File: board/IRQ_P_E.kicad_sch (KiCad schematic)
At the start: 8 parts, among them U60 CY7C192-25, U61 CY7C192-25, U85 ATF22V10C-10PU, U86 ATF22V10C-10PU

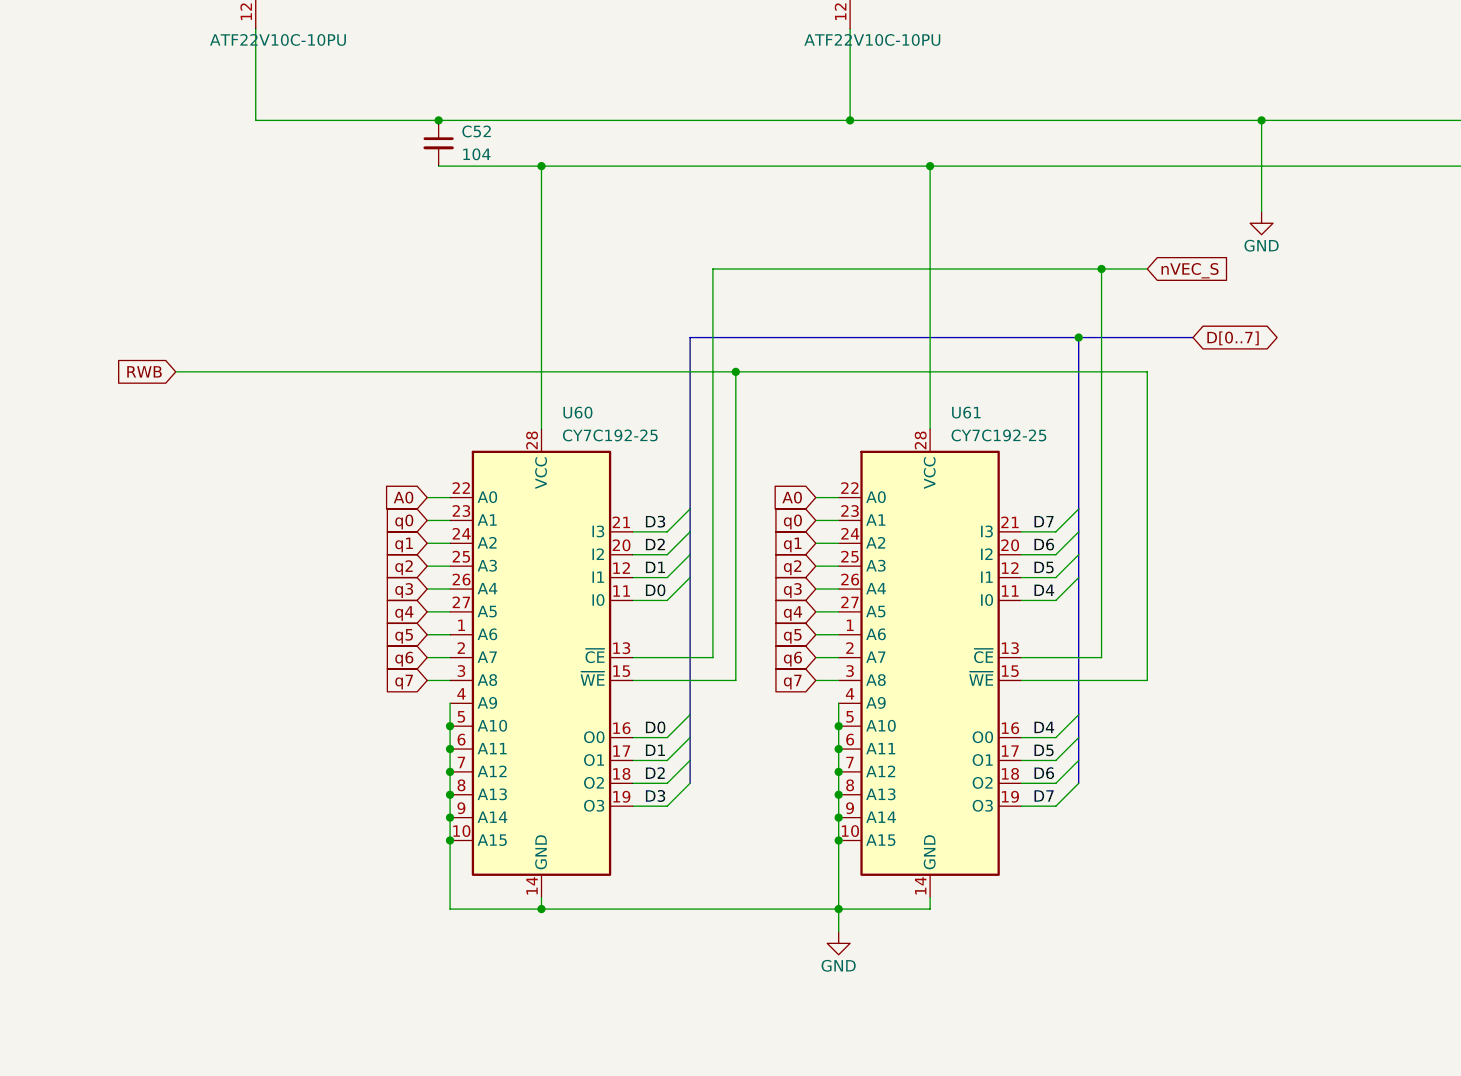
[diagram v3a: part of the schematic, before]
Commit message: V2.0: consolidate parts (239 -> 216), GAL C rev 02
No change in function:
- U9 74F08 removed: GAL C (U88) rev 02 makes the CPU phi0 (P_PHI0 = PHI2
  held low while DMAB_S is low); its decoupling cap C14 removed
- U34 74ACT14 removed: the two clock buffers use spare U19 74F240 gates
- U60 + U61 (2 x CY7C192 vector RAM) replaced by one AS7C256B-15
  (32K x 8, 15 ns); the IRQ sheet's D[0..7] bus is gone
- Crystal oscillators (U75 74HCU04, Y1, Y2, R1, R6-R8, C43, C44, C96,
  C97) replaced by canned oscillators X1 (14.31818 MHz), X2 (1.8432 MHz)
- Soft power: CD40106 -> 74HC14, CD4013 -> 74HC74 (active-low set/reset,
  power-on reset network inverted); a spare 74HC14 gate drives PS_ON#,
  so Q1 is removed
- R10-R13 -> RN6 (4 x 10k, SIP-5); R9, R21-R24 -> RN7 (5 x 33R isolated,
  SIP-10)
- C100-C102 (3 x 220u) -> C100 680u
- Clocks and Power sheet notes updated; PLD README updated

GAL C rev 02 verified against rev 01 over 200,000 clock edges.
PCB updated from the schematic (adds RN6, RN7, X1, X2 and the speakers
LS1/LS2). Also includes KiCad's re-save of the schematic sheets.

Co-Authored-By: Claude Opus 5.5 <noreply@anthropic.com>
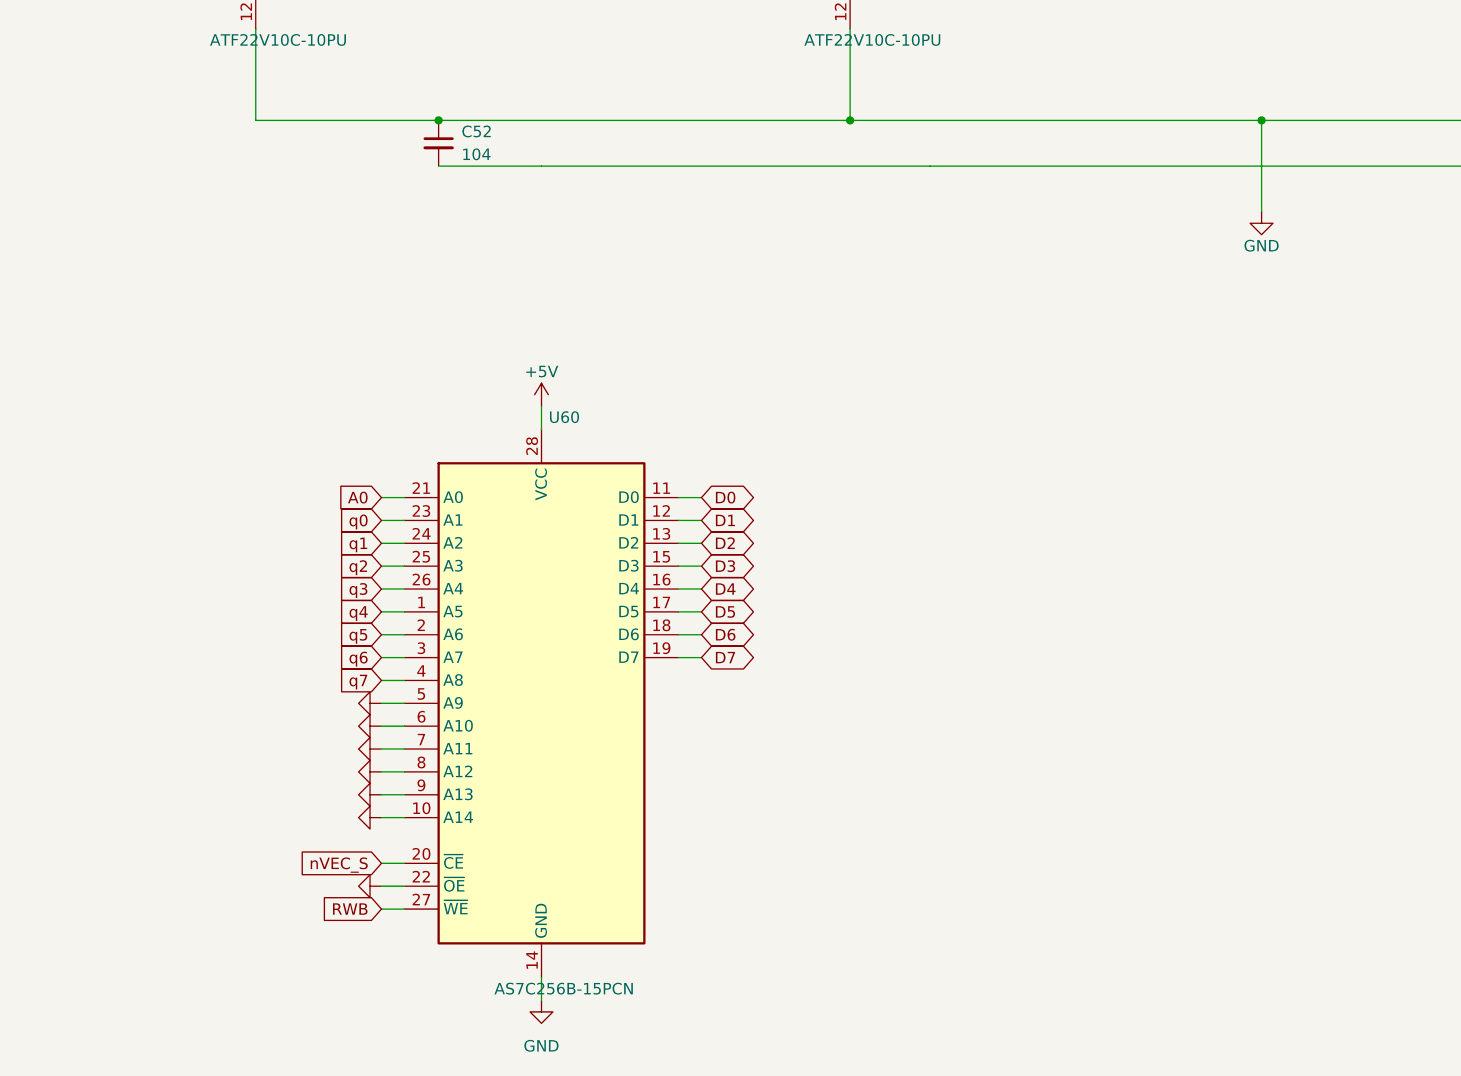
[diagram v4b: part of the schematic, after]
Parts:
- removed U61: CY7C192-25, Package_DIP:DIP-28_W7.62mm_Socket_LongPads, symbol Hydra16:CY7C192
- U60: value CY7C192-25 -> AS7C256B-15PCN; symbol Hydra16:CY7C192 -> Memory_RAM:CY7C199
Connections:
- net A0: now also U60.21 (A0); no longer U60.22 (A0)
- net D0: no longer U60.16 (O0)
- net D1: no longer U60.17 (O1)
- net D2: now also U60.13 (D2); no longer U60.18 (O2), U60.20 (I2)
- net D3: now also U60.15 (D3); no longer U60.19 (O3), U60.21 (I3)
- net D4: now also U60.16 (D4)
- net D5: now also U60.17 (D5)
- net D6: now also U60.18 (D6)
- net D7: now also U60.19 (D7)
- net GND: now also U60.22 (~{OE}); no longer U60.4 (A9)
- net RWB: now also U60.27 (~{WE}); no longer U60.15 (~{WE})
- net nVEC_S: now also U60.20 (~{CE}); no longer U60.13 (~{CE})
- net q4: now also U60.1 (A5); no longer U60.27 (A5)
- net q5: now also U60.2 (A6); no longer U60.1 (A6)
- net q6: now also U60.3 (A7); no longer U60.2 (A7)
- net q7: now also U60.4 (A8); no longer U60.3 (A8)
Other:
- moved on the sheet: U60
